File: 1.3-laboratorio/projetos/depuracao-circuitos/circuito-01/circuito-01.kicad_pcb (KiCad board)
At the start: 2 copper layers, 73.7 x 52.1 mm, 22 parts, among them J1 Conn_01x07_Male, J2 Conn_01x07_Male, J3 Conn_01x07_Male, J4 Conn_01x07_Male, J5 Conn_01x07_Male, J6 Conn_01x07_Male, J7 Conn_01x04, J8 Conn_01x04, P1 CONN_01X02, SW1 SW_DIP_x04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

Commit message: Leiaute quase finalizado para Circuito 01.
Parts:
- moved R4 19.1 mm to (157.5, 120.7), turned to 0 degrees
- moved R5 19.1 mm to (157.5, 124.5), turned to 0 degrees
- moved R2 8.98 mm to (182.9, 120.7)
- moved R3 8.98 mm to (182.9, 124.5)
- moved J8 3.42 mm to (162.6, 106.0)
- moved J7 3.42 mm to (177.8, 106.0)
- moved C1 1.27 mm to (158.8, 89.0)
- moved D1 1.27 mm to (149.9, 118.1)
- moved J1 1.27 mm to (162.6, 99.1)
- moved P1 1.27 mm to (148.6, 90.2)
- moved SW1 1.27 mm to (144.8, 97.8)
- moved U1 1.27 mm to (162.6, 95.2)
- moved J2 1.27 mm to (177.8, 83.8)
- moved R1 1.27 mm to (153.7, 111.5)
- moved C2 0.57 mm to (188.0, 89.0)
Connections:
- J7 pad 2: /U2-02 -> /U1-02
- J7 pad 3: /U1-06 -> /U2-02
- J8 pad 2: /U2-02 -> /U1-02
- J8 pad 3: /U1-06 -> /U2-02
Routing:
- net /U1-10: track 7.62 -> 52.8 mm, vias 0 -> 4
- net /U2-11: track 7.62 -> 52.0 mm, vias 0 -> 2
- net /U1-02: track 37.4 -> 68.6 mm
- net /U2-08: track 7.62 -> 36.3 mm, vias 0 -> 2
- net /U3-10: track 55.9 -> 28.8 mm
- net /U1-06: track 50.2 -> 38.0 mm, vias 0 -> 2
- net /U1-03: track 86.6 -> 94.5 mm
- net /U1-01: track 70.9 -> 78.1 mm
- net /U1-08: track 38.6 -> 43.9 mm
- net /U2-02: track 67.0 -> 71.0 mm
- net /U1-05: track 63.0 -> 60.8 mm
- net VCC: track 175.5 -> 177.2 mm
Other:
- board size 73.7 x 52.1 mm -> 76.2 x 54.6 mm

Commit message: Concluído o leiaute de Circuito 01.
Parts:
- J7, J8: value Conn_01x04 -> Conn_01x05; footprint Connector_PinSocket_2.54mm:PinSocket_1x04_P2.54mm_Vertical -> Connector_PinSocket_2.54mm:PinSocket_1x05_P2.54mm_Vertical
- moved D1 4.45 mm to (149.9, 122.6)
- moved R1 2.54 mm to (153.7, 114.0)
- moved J7 1.27 mm to (177.8, 104.8)
- moved J8 1.27 mm to (162.6, 104.8)
- moved SW1 1.27 mm to (144.8, 99.1)
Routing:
- net /U3-10: track 28.8 -> 57.3 mm, vias 0 -> 2
- net /U1-05: track 60.8 -> 66.5 mm
- net /U1-01: track 78.1 -> 73.6 mm
- net Net-(D1-Pad2): track 8.51 -> 11.6 mm
- net /U1-02: track 68.6 -> 67.5 mm
- net /U2-02: track 71.0 -> 72.0 mm

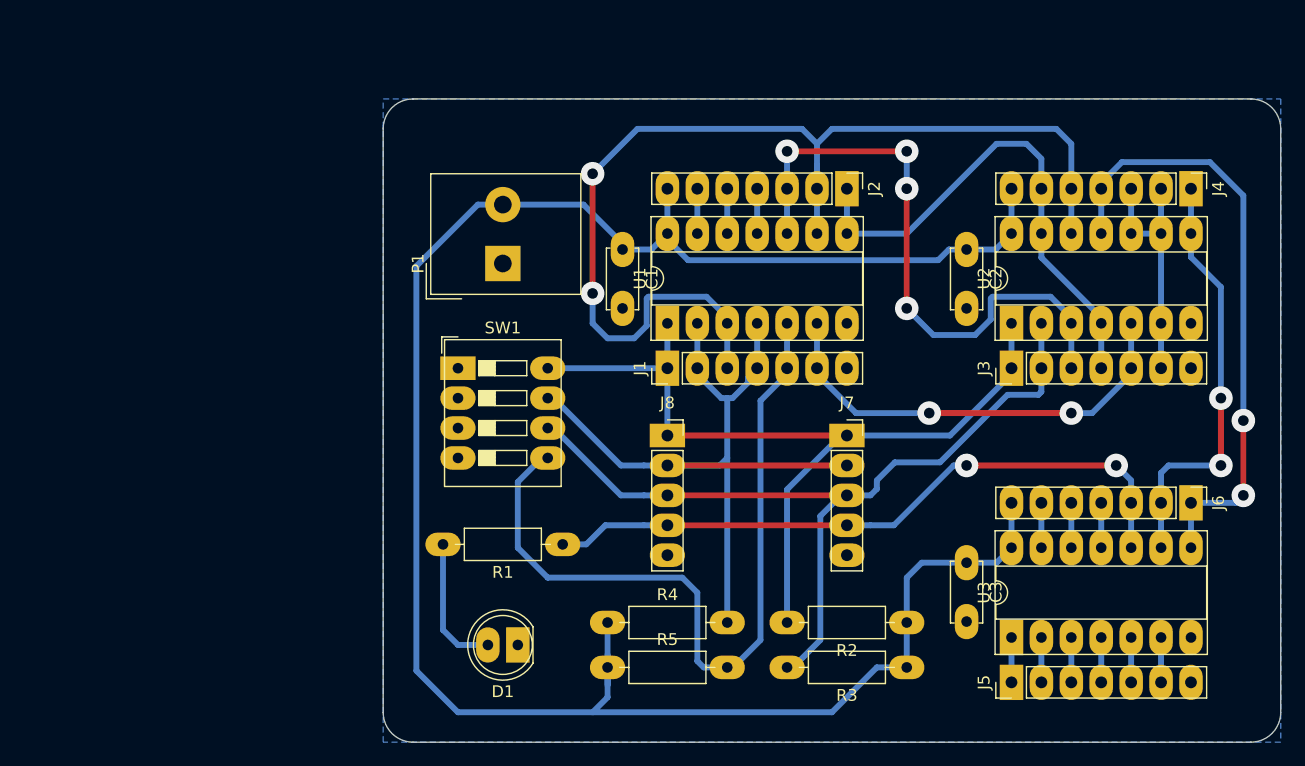
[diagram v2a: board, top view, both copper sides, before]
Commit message: Posicionamento das simbologias.
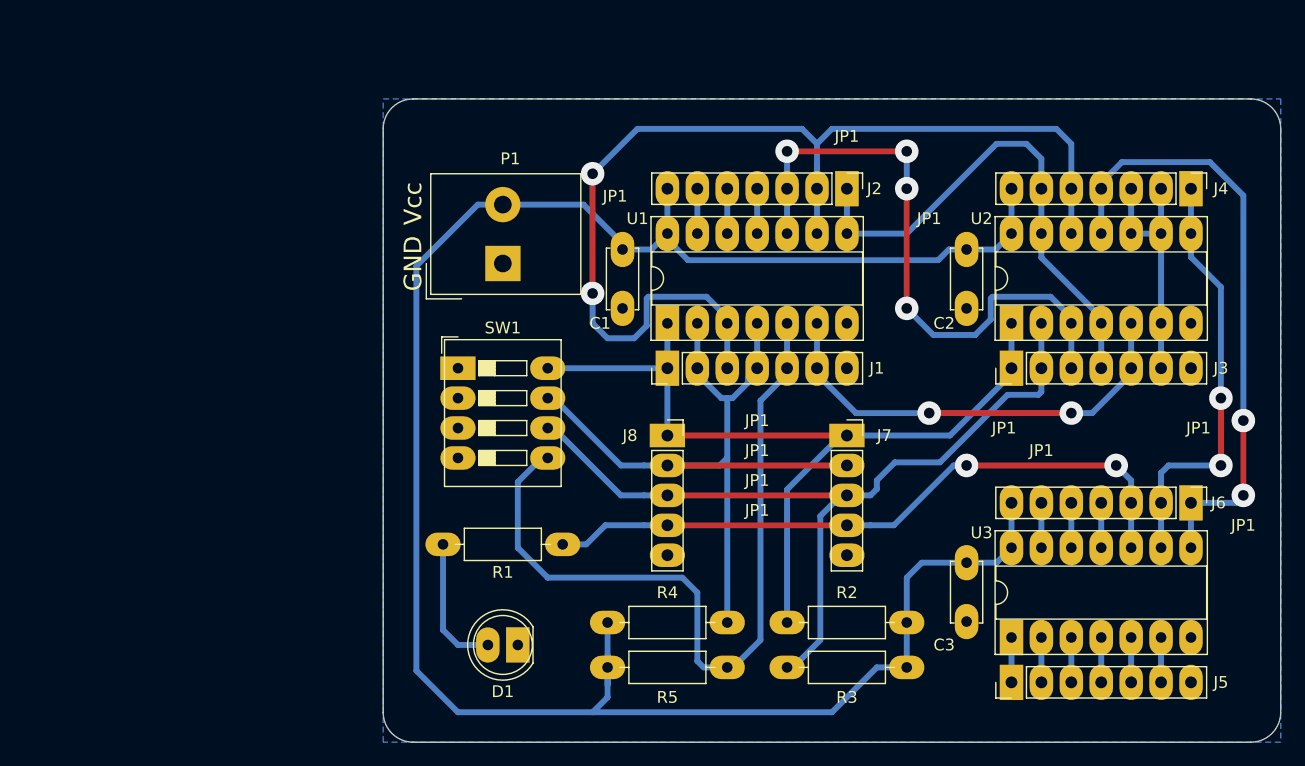
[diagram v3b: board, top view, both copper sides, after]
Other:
- board text added: "GND"
- board text added: "JP1"
- board text added: "Vcc"
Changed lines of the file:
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@@
   (general
     (thickness 1.6)
-    (drawings 12)
+    (drawings 25)
     (tracks 222)
     (zones 0)
@@
   (layers
     (0 F.Cu jumper)
-    (31 B.Cu signal)
+    (31 B.Cu signal hide)
     (33 F.Adhes user)
     (35 F.Paste user)
@@
     (uvia_min_size 0.2)
     (uvia_min_drill 0.1)
-    (pcb_text_width 0.3)
-    (pcb_text_size 1.5 1.5)
+    (pcb_text_width 0.15)
+    (pcb_text_size 1 1)
     (mod_edge_width 0.15)
     (mod_text_size 1 1)
@@
     (descr "Through hole straight socket strip, 1x05, 2.54mm pitch, single row (from Kicad 4.0.7), script generated")
     (tags "Through hole socket strip THT 1x05 2.54mm single row")
-    (fp_text reference J8 (at 0 -2.77) (layer F.SilkS)
+    (fp_text reference J8 (at -3.175 0) (layer F.SilkS)
       (effects (font (size 1 1) (thickness 0.15)))
     )
@@
     (descr "Through hole straight socket strip, 1x05, 2.54mm pitch, single row (from Kicad 4.0.7), script generated")
     (tags "Through hole socket strip THT 1x05 2.54mm single row")
-    (fp_text reference J7 (at 0 -2.77) (layer F.SilkS)
+    (fp_text reference J7 (at 3.175 0) (layer F.SilkS)
       (effects (font (size 1 1) (thickness 0.15)))
     )
@@
     (descr "C, Disc series, Radial, pin pitch=5.00mm, , diameter*width=5*2.5mm^2, Capacitor, http://cdn-reichelt.de/documents/datenblatt/B300/DS_KERKO_TC.pdf")
     (tags "C Disc series Radial pin pitch 5.00mm  diameter 5mm width 2.5mm Capacitor")
-    (fp_text reference C2 (at 2.5 -2.5 270) (layer F.SilkS)
+    (fp_text reference C2 (at 6.27 1.905) (layer F.SilkS)
       (effects (font (size 1 1) (thickness 0.15)))
     )
@@
     (descr "Through hole straight pin header, 1x07, 2.54mm pitch, single row")
     (tags "Through hole pin header THT 1x07 2.54mm single row")
-    (fp_text reference J1 (at 0 -2.33 90) (layer F.SilkS)
+    (fp_text reference J1 (at 0 17.78) (layer F.SilkS)
       (effects (font (size 1 1) (thickness 0.15)))
     )
@@
     (descr "Through hole straight pin header, 1x07, 2.54mm pitch, single row")
     (tags "Through hole pin header THT 1x07 2.54mm single row")
-    (fp_text reference J2 (at 0 -2.33 270) (layer F.SilkS)
+    (fp_text reference J2 (at 0 -2.33) (layer F.SilkS)
       (effects (font (size 1 1) (thickness 0.15)))
     )
@@
     (descr "Through hole straight pin header, 1x07, 2.54mm pitch, single row")
     (tags "Through hole pin header THT 1x07 2.54mm single row")
-    (fp_text reference J3 (at 0 -2.33 90) (layer F.SilkS)
+    (fp_text reference J3 (at 0 17.78 180) (layer F.SilkS)
       (effects (font (size 1 1) (thickness 0.15)))
     )
@@
     (descr "Through hole straight pin header, 1x07, 2.54mm pitch, single row")
     (tags "Through hole pin header THT 1x07 2.54mm single row")
-    (fp_text reference J4 (at 0 -2.33 270) (layer F.SilkS)
+    (fp_text reference J4 (at 0 -2.54) (layer F.SilkS)
       (effects (font (size 1 1) (thickness 0.15)))
     )
@@
     (descr "Through hole straight pin header, 1x07, 2.54mm pitch, single row")
     (tags "Through hole pin header THT 1x07 2.54mm single row")
-    (fp_text reference J5 (at 0 -2.33 90) (layer F.SilkS)
+    (fp_text reference J5 (at 0 17.78 180) (layer F.SilkS)
       (effects (font (size 1 1) (thickness 0.15)))
     )
@@
     (descr "Through hole straight pin header, 1x07, 2.54mm pitch, single row")
     (tags "Through hole pin header THT 1x07 2.54mm single row")
-    (fp_text reference J6 (at 0 -2.33 270) (layer F.SilkS)
+    (fp_text reference J6 (at 0 -2.33) (layer F.SilkS)
       (effects (font (size 1 1) (thickness 0.15)))
     )
@@
     (descr "Altech AK300 serie terminal block (Script generated with StandardBox.py) (http://www.altechcorp.com/PDFS/PCBMETRC.PDF)")
     (tags "Altech AK300 serie connector")
-    (fp_text reference P1 (at 0 -7.2 90) (layer F.SilkS)
+    (fp_text reference P1 (at 8.89 0.635) (layer F.SilkS)
       (effects (font (size 1 1) (thickness 0.15)))
     )
@@
     (descr "Resistor, Axial_DIN0207 series, Axial, Horizontal, pin pitch=10.16mm, 0.25W = 1/4W, length*diameter=6.3*2.5mm^2, http://cdn-reichelt.de/documents/datenblatt/B400/1_4W%23YAG.pdf")
     (tags "Resistor Axial_DIN0207 series Axial Horizontal pin pitch 10.16mm 0.25W = 1/4W length 6.3mm diameter 2.5mm")
-    (fp_text reference R2 (at 5.08 -2.37 180) (layer F.SilkS)
+    (fp_text reference R2 (at 5.08 2.54 180) (layer F.SilkS)
       (effects (font (size 1 1) (thickness 0.15)))
     )
@@
     (descr "Resistor, Axial_DIN0207 series, Axial, Horizontal, pin pitch=10.16mm, 0.25W = 1/4W, length*diameter=6.3*2.5mm^2, http://cdn-reichelt.de/documents/datenblatt/B400/1_4W%23YAG.pdf")
     (tags "Resistor Axial_DIN0207 series Axial Horizontal pin pitch 10.16mm 0.25W = 1/4W length 6.3mm diameter 2.5mm")
-    (fp_text reference R3 (at 5.08 -2.37 180) (layer F.SilkS)
+    (fp_text reference R3 (at 5.08 -2.54 180) (layer F.SilkS)
       (effects (font (size 1 1) (thickness 0.15)))
     )
@@
     (descr "Resistor, Axial_DIN0207 series, Axial, Horizontal, pin pitch=10.16mm, 0.25W = 1/4W, length*diameter=6.3*2.5mm^2, http://cdn-reichelt.de/documents/datenblatt/B400/1_4W%23YAG.pdf")
     (tags "Resistor Axial_DIN0207 series Axial Horizontal pin pitch 10.16mm 0.25W = 1/4W length 6.3mm diameter 2.5mm")
-    (fp_text reference R4 (at 5.08 -2.37) (layer F.SilkS)
+    (fp_text reference R4 (at 5.08 -2.54) (layer F.SilkS)
       (effects (font (size 1 1) (thickness 0.15)))
     )
@@
     (descr "Resistor, Axial_DIN0207 series, Axial, Horizontal, pin pitch=10.16mm, 0.25W = 1/4W, length*diameter=6.3*2.5mm^2, http://cdn-reichelt.de/documents/datenblatt/B400/1_4W%23YAG.pdf")
     (tags "Resistor Axial_DIN0207 series Axial Horizontal pin pitch 10.16mm 0.25W = 1/4W length 6.3mm diameter 2.5mm")
-    (fp_text reference R5 (at 5.08 -2.37) (layer F.SilkS)
+    (fp_text reference R5 (at 5.08 2.54) (layer F.SilkS)
       (effects (font (size 1 1) (thickness 0.15)))
     )
@@
     (descr "14-lead though-hole mounted DIP package, row spacing 7.62 mm (300 mils), Socket, LongPads")
     (tags "THT DIP DIL PDIP 2.54mm 7.62mm 300mil Socket LongPads")
-    (fp_text reference U1 (at 3.81 -2.33 90) (layer F.SilkS)
+    (fp_text reference U1 (at 8.89 -2.54 180) (layer F.SilkS)
       (effects (font (size 1 1) (thickness 0.15)))
     )
@@
     (descr "14-lead though-hole mounted DIP package, row spacing 7.62 mm (300 mils), Socket, LongPads")
     (tags "THT DIP DIL PDIP 2.54mm 7.62mm 300mil Socket LongPads")
-    (fp_text reference U2 (at 3.81 -2.33 90) (layer F.SilkS)
+    (fp_text reference U2 (at 8.89 -2.54 180) (layer F.SilkS)
       (effects (font (size 1 1) (thickness 0.15)))
     )
@@
     (descr "14-lead though-hole mounted DIP package, row spacing 7.62 mm (300 mils), Socket, LongPads")
     (tags "THT DIP DIL PDIP 2.54mm 7.62mm 300mil Socket LongPads")
-    (fp_text reference U3 (at 3.81 -2.33 90) (layer F.SilkS)
+    (fp_text reference U3 (at 8.89 -2.54 180) (layer F.SilkS)
       (effects (font (size 1 1) (thickness 0.15)))
     )
@@
     (descr "C, Disc series, Radial, pin pitch=5.00mm, , diameter*width=5*2.5mm^2, Capacitor, http://cdn-reichelt.de/documents/datenblatt/B300/DS_KERKO_TC.pdf")
     (tags "C Disc series Radial pin pitch 5.00mm  diameter 5mm width 2.5mm Capacitor")
-    (fp_text reference C1 (at 2.5 -2.5 270) (layer F.SilkS)
+    (fp_text reference C1 (at 6.27 1.905) (layer F.SilkS)
       (effects (font (size 1 1) (thickness 0.15)))
     )
@@
     (descr "C, Disc series, Radial, pin pitch=5.00mm, , diameter*width=5*2.5mm^2, Capacitor, http://cdn-reichelt.de/documents/datenblatt/B300/DS_KERKO_TC.pdf")
     (tags "C Disc series Radial pin pitch 5.00mm  diameter 5mm width 2.5mm Capacitor")
-    (fp_text reference C3 (at 2.5 -2.5 270) (layer F.SilkS)
+    (fp_text reference C3 (at 6.985 1.905 180) (layer F.SilkS)
       (effects (font (size 1 1) (thickness 0.15)))
     )
@@
     )
   )
+  (gr_text JP1 (at 211.455 112.395) (layer F.SilkS)
+    (effects (font (size 1 1) (thickness 0.15)))
+  )
+  (gr_text JP1 (at 207.645 104.14) (layer F.SilkS)
+    (effects (font (size 1 1) (thickness 0.15)))
+  )
+  (gr_text JP1 (at 194.31 106.045) (layer F.SilkS)
+    (effects (font (size 1 1) (thickness 0.15)))
+  )
+  (gr_text JP1 (at 191.135 104.14) (layer F.SilkS)
+    (effects (font (size 1 1) (thickness 0.15)))
+  )
+  (gr_text JP1 (at 170.18 111.125) (layer F.SilkS)
+    (effects (font (size 1 1) (thickness 0.15)))
+  )
+  (gr_text JP1 (at 170.18 108.585) (layer F.SilkS)
+    (effects (font (size 1 1) (thickness 0.15)))
+  )
+  (gr_text JP1 (at 170.18 106.045) (layer F.SilkS)
+    (effects (font (size 1 1) (thickness 0.15)))
+  )
+  (gr_text JP1 (at 170.18 103.505) (layer F.SilkS)
+    (effects (font (size 1 1) (thickness 0.15)))
+  )
+  (gr_text JP1 (at 184.785 86.36) (layer F.SilkS)
+    (effects (font (size 1 1) (thickness 0.15)))
+  )
+  (gr_text JP1 (at 177.8 79.375) (layer F.SilkS)
+    (effects (font (size 1 1) (thickness 0.15)))
+  )
+  (gr_text JP1 (at 158.115 84.455) (layer F.SilkS)
+    (effects (font (size 1 1) (thickness 0.15)))
+  )
+  (gr_text GND (at 140.97 90.17 90) (layer F.SilkS)
+    (effects (font (size 1.5 1.5) (thickness 0.2)))
+  )
+  (gr_text Vcc (at 140.97 85.09 90) (layer F.SilkS)
+    (effects (font (size 1.5 1.5) (thickness 0.2)))
+  )
   (gr_arc (start 212.09 128.27) (end 212.09 130.81) (angle -90) (layer Edge.Cuts) (width 0.1))

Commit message: Concluída a edição das simbologias da placa e de fabricação.
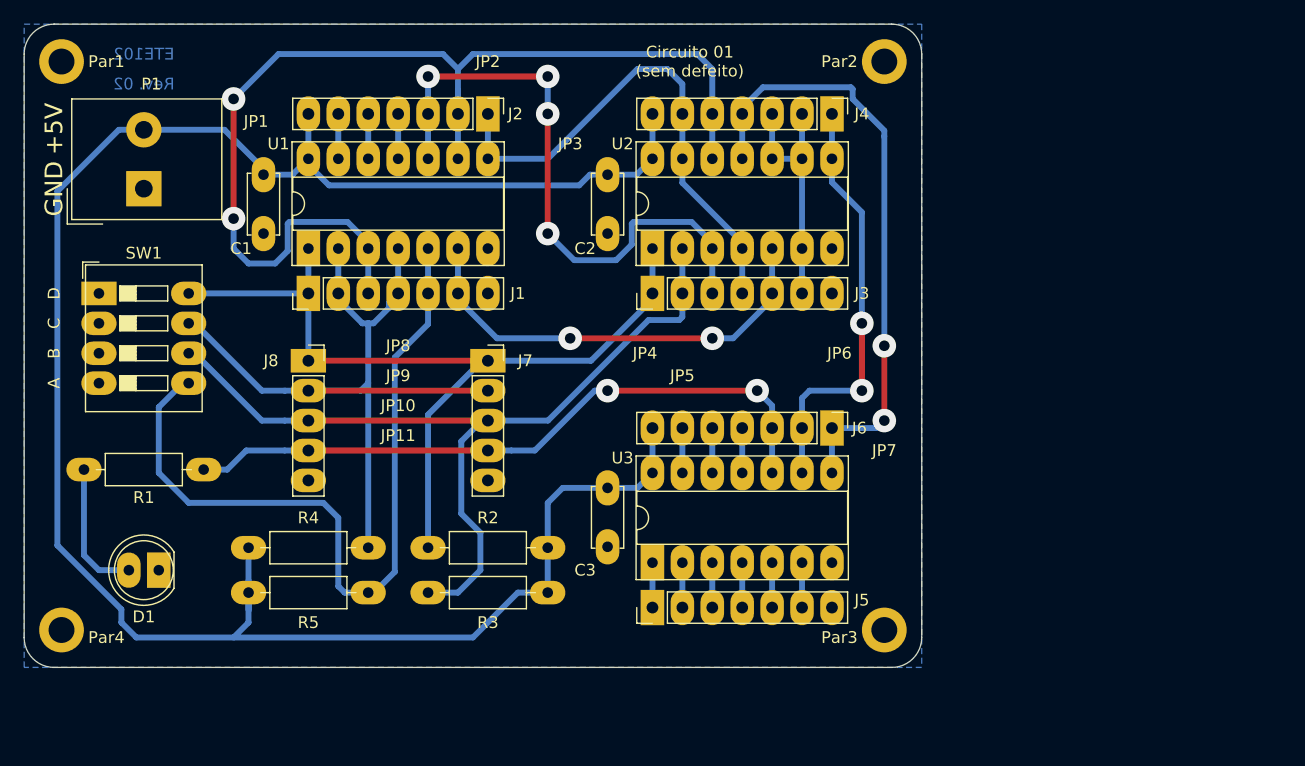
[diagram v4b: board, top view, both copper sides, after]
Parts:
- added Par1: MountingHole_2.2mm_M2_ISO14580_Pad, MountingHole:MountingHole_2.2mm_M2_ISO14580_Pad, F.Cu at (111.1, 73.0)
- added Par2: MountingHole_2.2mm_M2_ISO14580_Pad, MountingHole:MountingHole_2.2mm_M2_ISO14580_Pad, F.Cu at (181.0, 73.0)
- added Par3: MountingHole_2.2mm_M2_ISO14580_Pad, MountingHole:MountingHole_2.2mm_M2_ISO14580_Pad, F.Cu at (181.0, 121.3)
- added Par4: MountingHole_2.2mm_M2_ISO14580_Pad, MountingHole:MountingHole_2.2mm_M2_ISO14580_Pad, F.Cu at (111.1, 121.3)
- D1: value LED_ALT -> LED_VD
- moved C2 31.1 mm to (157.5, 82.6)
- moved C3 31.1 mm to (157.5, 109.2)
- moved D1 31.1 mm to (119.4, 116.2)
- moved J2 31.1 mm to (147.3, 77.5)
- moved J3 31.1 mm to (161.3, 92.7)
- moved J5 31.1 mm to (161.3, 119.4)
- moved J7 31.1 mm to (147.3, 98.4)
- moved U2 31.1 mm to (161.3, 88.9)
- moved U3 31.1 mm to (161.3, 115.6)
- moved P1 31.1 mm to (118.1, 83.8)
- moved SW1 31.1 mm to (114.3, 92.7)
- moved C1 31.1 mm to (128.3, 82.6)
- moved J1 31.1 mm to (132.1, 92.7)
- moved J4 31.1 mm to (176.5, 77.5)
- moved J6 31.1 mm to (176.5, 104.1)
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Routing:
- net /U2-02: track 72.0 -> 74.1 mm
- net VCC: track 177.2 -> 175.4 mm
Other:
- board text added: "+5V"
- board text added: "A"
- board text added: "B"
- board text added: "C"
- board text added: "Circuito 01 (sem defeito)"
- board text added: "D"
- board text added: "ETE102"
- board text added: "JP10"
- board text added: "JP11"
- board text added: "JP2"
- board text added: "JP3"
- board text added: "JP4"
- board text added: "JP5"
- board text added: "JP6"
- board text added: "JP7"
- board text added: "JP8"
- board text added: "JP9"
- board text added: "Rev. 02"
- board text removed: "Vcc"

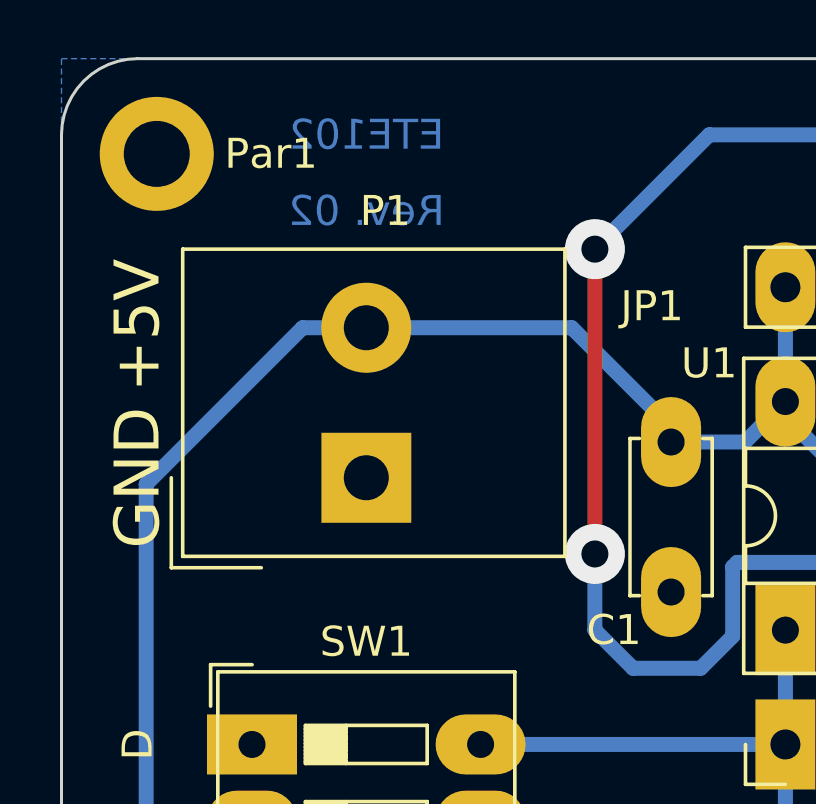
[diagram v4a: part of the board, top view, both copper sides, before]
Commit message: Exibição 3D corrigida do Circuito 01 para depuração. Dados experimentais para a experiência de Teoremas de Thévenin, Norton e da Superposição. Criação de subdiretório com ícone e imagem de PCI.
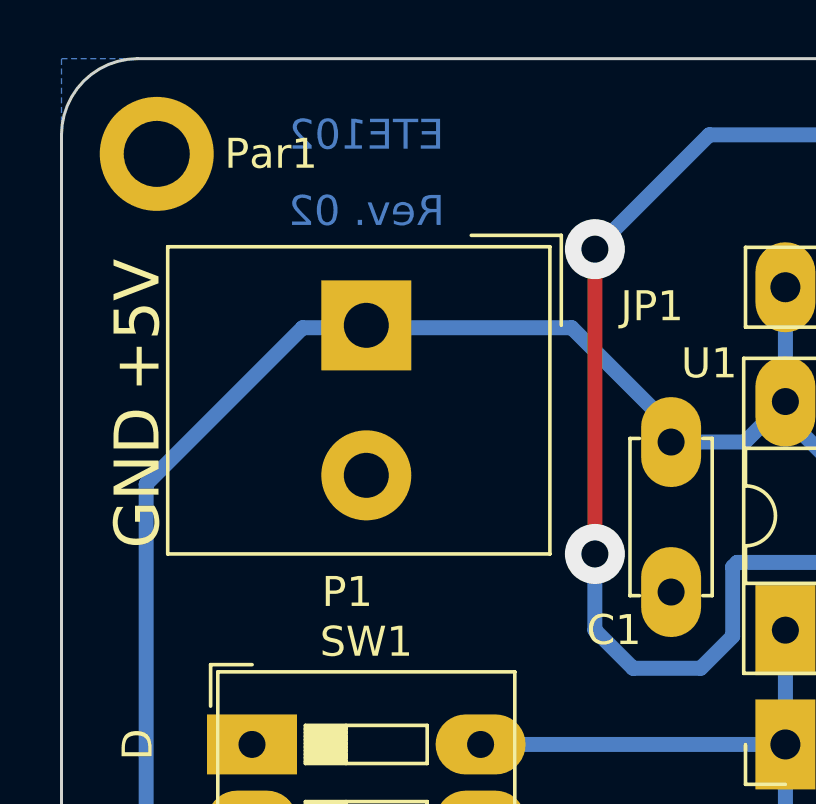
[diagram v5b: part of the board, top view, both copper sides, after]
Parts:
- D1: value LED_VD -> LED_ALT
- moved P1 5.08 mm to (118.1, 78.7), turned to 270 degrees
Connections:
- P1 pad 1: GND -> VCC
- P1 pad 2: VCC -> GND
